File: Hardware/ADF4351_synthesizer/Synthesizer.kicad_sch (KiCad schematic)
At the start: 48 parts, among them J5 SMA-J-P-H-ST-EM1, J6 Conn_Coaxial, J7 Conn_Coaxial, U5 ADF4351, X2 XO32

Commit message: Updating schematic
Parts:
- removed R22, R23: 10k, Resistor_SMD:R_0603_1608Metric, symbol Device:R_Small_US
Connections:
- net +3.3VA: now also U5.26 (PDB_RF), U5.4 (CE)
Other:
- note added: "ADM7150ARDZ-3.3-R7"
- moved on the sheet: C46, C69, C70, C71, C75, C76, J5, J6, J7, L10, L11, L14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

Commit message: Updating schematic
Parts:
- removed J7: Conn_Coaxial, symbol Connector:Conn_Coaxial
- added J2: SMA-J-P-H-ST-EM1, Connector_Coaxial:SMA_Samtec_SMA-J-P-X-ST-EM1_EdgeMount, symbol Connector:Conn_Coaxial
- added R10: 5.1k, Resistor_SMD:R_0603_1608Metric, symbol Device:R_Small_US
- J6: value Conn_Coaxial -> SMA-J-P-H-ST-EM1; footprint (none) -> Connector_Coaxial:SMA_Samtec_SMA-J-P-X-ST-EM1_EdgeMount; Digikey (none) -> SAM8857-ND
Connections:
- net +3.3VA: now also R10.1
- net GND: now also J2.2 (Ext)
- net RF+: now also J2.1 (In)
- net XO_EN: now also R10.2
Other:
- moved on the sheet: C46, D7, J5, R21, R25, R29

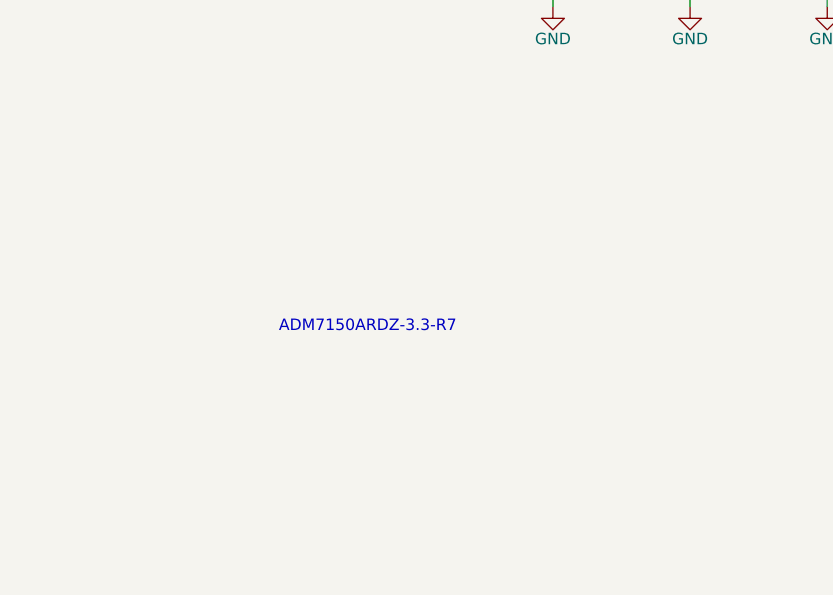
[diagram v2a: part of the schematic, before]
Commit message: Adding low noise regulator to schematic
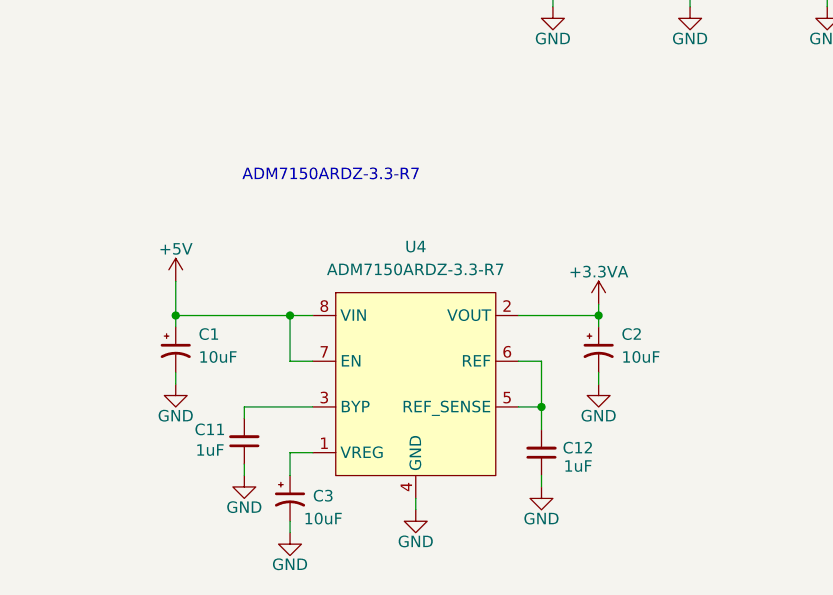
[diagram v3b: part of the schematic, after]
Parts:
- added C1, C2, C3: 10uF, Capacitor_Tantalum_SMD:CP_EIA-3216-18_Kemet-A, symbol Device:C_Polarized_Small_US
- added C11, C12: 1uF, Capacitor_SMD:C_0402_1005Metric, symbol Device:C_Small
- added U4: ADM7150ARDZ-3.3-R7, Package_SO:SOIC-8-1EP_3.9x4.9mm_P1.27mm_EP2.29x3mm, symbol _tim-DC_DC:ADM7150ARDZ-3.3-R7
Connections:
- net +3.3VA: now also C2.1, U4.2 (VOUT)
- net GND: now also C1.2, C11.1, C12.1, C2.2, C3.2, U4.4 (GND), U4.9 (EP)
- new net: C3.1, U4.1 (VREG)
- new net: C11.2, U4.3 (BYP)
- new net: C12.2, U4.5 (REF_SENSE), U4.6 (REF)
- new net +5V: C1.1, U4.7 (EN), U4.8 (VIN)

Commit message: Starting to organize PCB Layout
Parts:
- J3: renamed from J5; footprint Connector_Coaxial:SMA_Samtec_SMA-J-P-X-ST-EM1_EdgeMount -> Connector_Coaxial:SMA_Samtec_SMA-J-P-H-ST-EM1_EdgeMount
- J4: renamed from J2; footprint Connector_Coaxial:SMA_Samtec_SMA-J-P-X-ST-EM1_EdgeMount -> Connector_Coaxial:SMA_Samtec_SMA-J-P-H-ST-EM1_EdgeMount
- J5: renamed from J6; footprint Connector_Coaxial:SMA_Samtec_SMA-J-P-X-ST-EM1_EdgeMount -> Connector_Coaxial:SMA_Samtec_SMA-J-P-H-ST-EM1_EdgeMount
- renumbered C11 to C10, C3 to C11, C47 to C12, C12 to C13, C48 to C14, C2 to C15, C49 to C16, C50 to C17, C51 to C18, C52 to C19, C53 to C20, C54 to C21, C55 to C22, C56 to C23, C57 to C24, C58 to C25, C59 to C26, C60 to C27, C61 to C28, C62 to C29, C63 to C30, C64 to C31, C65 to C32, C66 to C33, C67 to C34, C68 to C35, C69 to C36, C70 to C37, C71 to C38, C75 to C39, C76 to C40, C46 to C8, C1 to C9, D7 to D3, L10 to L1, L11 to L2, L14 to L3, L15 to L4, R25 to R10, R26 to R11, R27 to R12, R29 to R13, R28 to R14, R10 to R6, R20 to R7, R21 to R8, R24 to R9, U4 to U3, U5 to U4, X2 to X1
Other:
- note added: "Low Noise Regulator"
- note added: "Reference"
- note removed: "ADM7150ARDZ-3.3-R7"
- moved on the sheet: C10, C11, C12, C13, C14, C15, C16, C17, C18, C19, C20, C21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

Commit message: Updating board
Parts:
- added C2: 100nF, Capacitor_SMD:C_0402_1005Metric, symbol Device:C_Small
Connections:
- net +3.3VA: now also C2.1
- net GND: now also C2.2
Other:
- moved on the sheet: C36, C37, C38, C39, C40, J4, J5, L1, L2, L3, L4
